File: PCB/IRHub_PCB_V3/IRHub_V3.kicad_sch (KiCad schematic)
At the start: 85 parts, among them Q1 UMH3N, SW1 SW_Push, U1 DRV2605LDGS

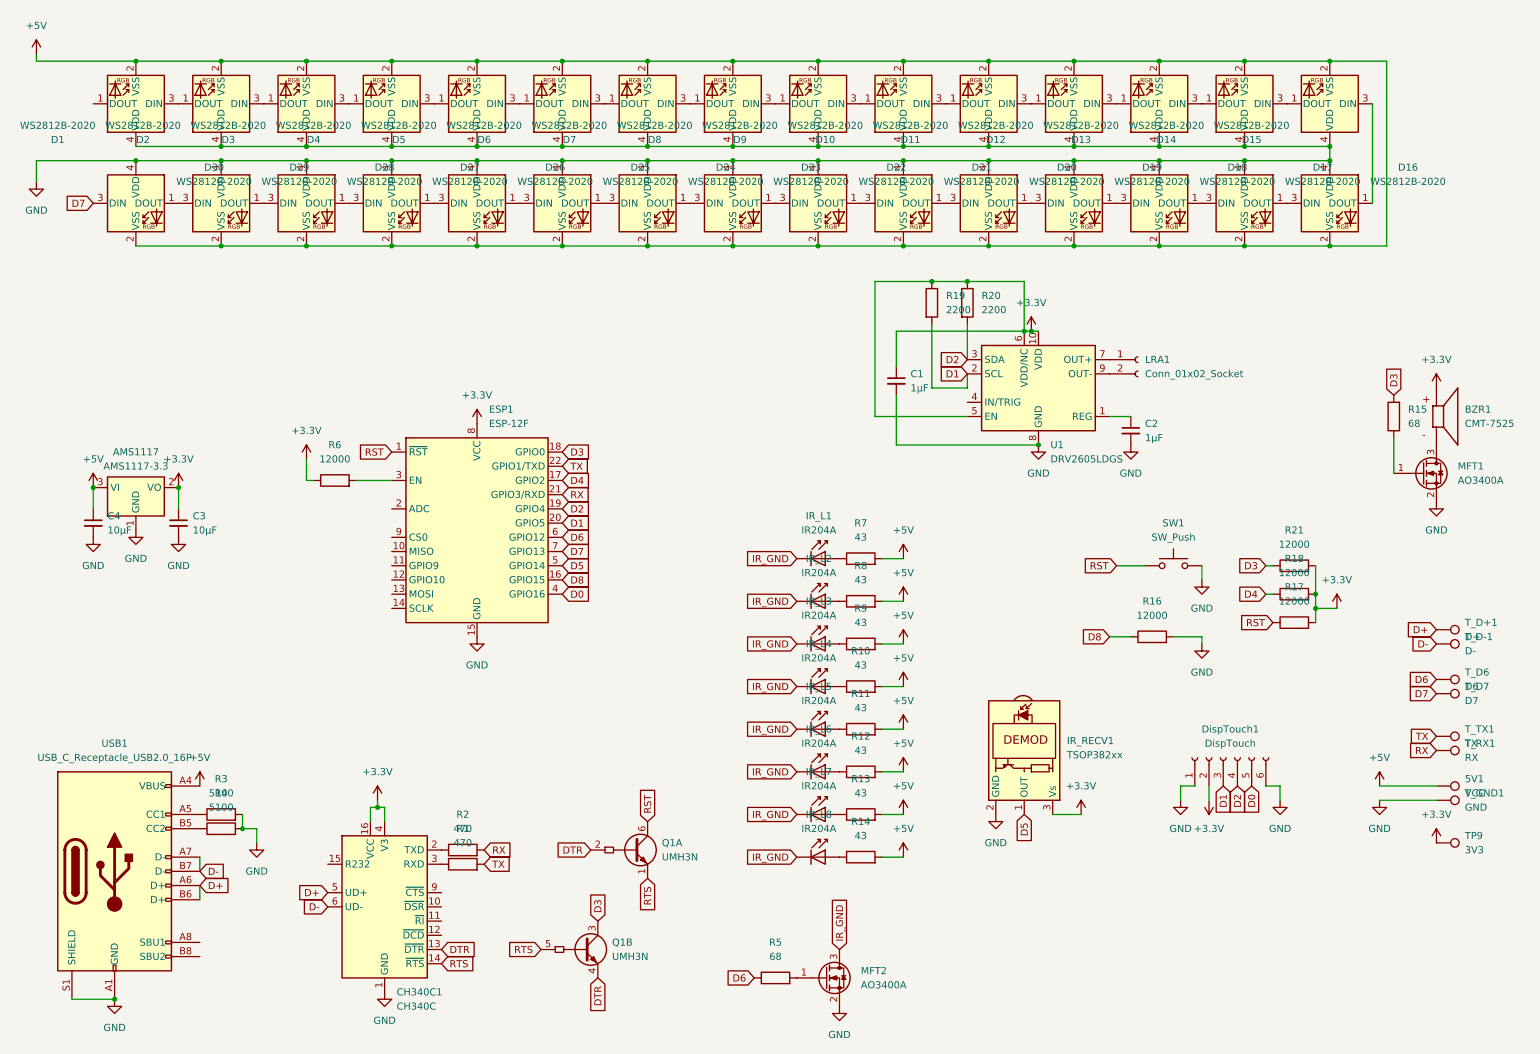
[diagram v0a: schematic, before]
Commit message: fix pcb led issue :)
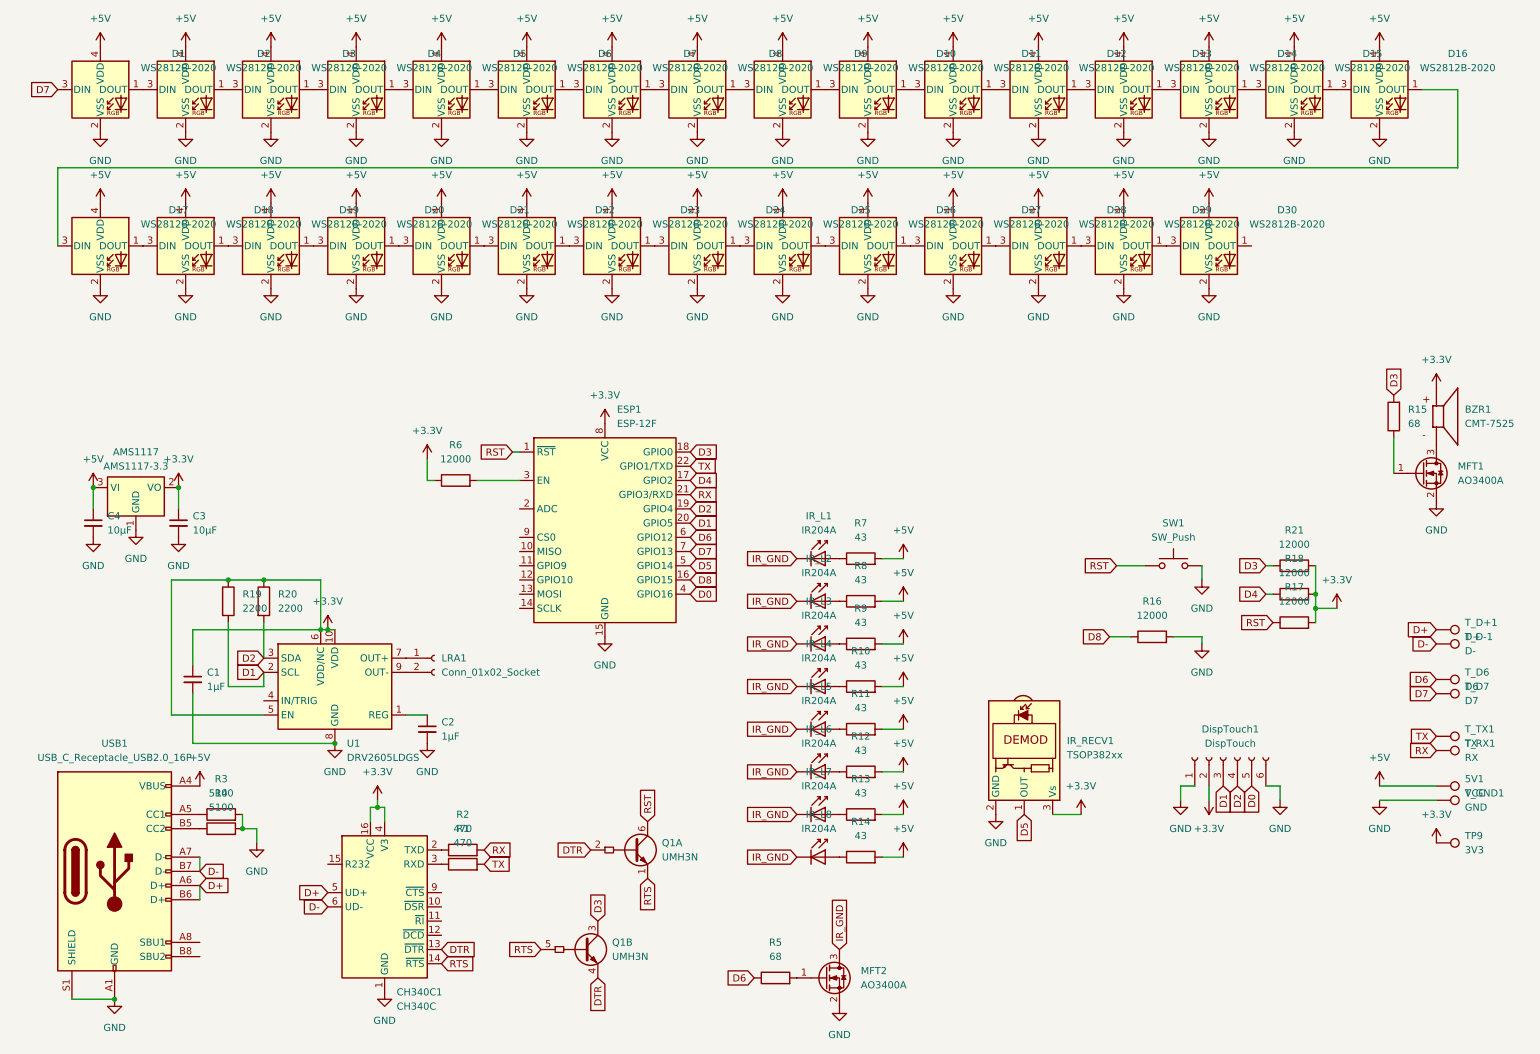
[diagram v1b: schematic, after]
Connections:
- net +5V: now also D1.4 (VDD), D10.4 (VDD), D11.4 (VDD), D12.4 (VDD), D13.4 (VDD), D14.4 (VDD), D15.4 (VDD), D16.4 (VDD), D17.4 (VDD), D18.4 (VDD), D19.4 (VDD), D2.4 (VDD), D20.4 (VDD), D21.4 (VDD), D22.4 (VDD), D23.4 (VDD), D24.4 (VDD), D25.4 (VDD), D26.4 (VDD), D27.4 (VDD), D28.4 (VDD), D29.4 (VDD), D3.4 (VDD), D30.4 (VDD), D4.4 (VDD), D5.4 (VDD), D6.4 (VDD), D7.4 (VDD), D8.4 (VDD), D9.4 (VDD); no longer D1.2 (VSS), D10.2 (VSS), D11.2 (VSS), D12.2 (VSS), D13.2 (VSS), D14.2 (VSS), D15.2 (VSS), D16.2 (VSS), D17.2 (VSS), D18.2 (VSS), D19.2 (VSS), D2.2 (VSS), D20.2 (VSS), D21.2 (VSS), D22.2 (VSS), D23.2 (VSS), D24.2 (VSS), D25.2 (VSS), D26.2 (VSS), D27.2 (VSS), D28.2 (VSS), D29.2 (VSS), D3.2 (VSS), D30.2 (VSS), D4.2 (VSS), D5.2 (VSS), D6.2 (VSS), D7.2 (VSS), D8.2 (VSS), D9.2 (VSS)
- net D7: now also D1.3 (DIN); no longer D30.3 (DIN)
- net GND: now also D1.2 (VSS), D10.2 (VSS), D11.2 (VSS), D12.2 (VSS), D13.2 (VSS), D14.2 (VSS), D15.2 (VSS), D16.2 (VSS), D17.2 (VSS), D18.2 (VSS), D19.2 (VSS), D2.2 (VSS), D20.2 (VSS), D21.2 (VSS), D22.2 (VSS), D23.2 (VSS), D24.2 (VSS), D25.2 (VSS), D26.2 (VSS), D27.2 (VSS), D28.2 (VSS), D29.2 (VSS), D3.2 (VSS), D30.2 (VSS), D4.2 (VSS), D5.2 (VSS), D6.2 (VSS), D7.2 (VSS), D8.2 (VSS), D9.2 (VSS); no longer D1.4 (VDD), D10.4 (VDD), D11.4 (VDD), D12.4 (VDD), D13.4 (VDD), D14.4 (VDD), D15.4 (VDD), D16.4 (VDD), D17.4 (VDD), D18.4 (VDD), D19.4 (VDD), D2.4 (VDD), D20.4 (VDD), D21.4 (VDD), D22.4 (VDD), D23.4 (VDD), D24.4 (VDD), D25.4 (VDD), D26.4 (VDD), D27.4 (VDD), D28.4 (VDD), D29.4 (VDD), D3.4 (VDD), D30.4 (VDD), D4.4 (VDD), D5.4 (VDD), D6.4 (VDD), D7.4 (VDD), D8.4 (VDD), D9.4 (VDD)
- net at D29.1 (DOUT): now also D30.3 (DIN); no longer D28.3 (DIN)
- net at D29.3 (DIN): now also D28.1 (DOUT); no longer D30.1 (DOUT)
- net at D1.1 (DOUT): now also D2.3 (DIN)
- net at D2.1 (DOUT): now also D3.3 (DIN); no longer D1.3 (DIN)
- net at D19.1 (DOUT): now also D20.3 (DIN); no longer D18.3 (DIN)
- net at D20.1 (DOUT): now also D21.3 (DIN); no longer D19.3 (DIN)
- net at D8.1 (DOUT): now also D9.3 (DIN); no longer D7.3 (DIN)
- net at D9.1 (DOUT): now also D10.3 (DIN); no longer D8.3 (DIN)
- net at D17.3 (DIN): now also D16.1 (DOUT); no longer D18.1 (DOUT)
- net at D21.1 (DOUT): now also D22.3 (DIN); no longer D20.3 (DIN)
- net at D26.3 (DIN): now also D25.1 (DOUT); no longer D27.1 (DOUT)
- net at D27.3 (DIN): now also D26.1 (DOUT); no longer D28.1 (DOUT)
- net at D10.1 (DOUT): now also D11.3 (DIN); no longer D9.3 (DIN)
- net at D11.1 (DOUT): now also D12.3 (DIN); no longer D10.3 (DIN)
- net at D6.3 (DIN): now also D5.1 (DOUT); no longer D7.1 (DOUT)
- net at D13.1 (DOUT): now also D14.3 (DIN); no longer D12.3 (DIN)
- net at D14.1 (DOUT): now also D15.3 (DIN); no longer D13.3 (DIN)
- net at D5.3 (DIN): now also D4.1 (DOUT); no longer D6.1 (DOUT)
- net at D23.3 (DIN): now also D22.1 (DOUT); no longer D24.1 (DOUT)
- net at D24.3 (DIN): now also D23.1 (DOUT); no longer D25.1 (DOUT)
- net at D3.1 (DOUT): now also D4.3 (DIN); no longer D2.3 (DIN)
- net at D15.1 (DOUT): now also D16.3 (DIN); no longer D14.3 (DIN)
- net at D12.1 (DOUT): now also D13.3 (DIN); no longer D11.3 (DIN)
- net at D25.3 (DIN): now also D24.1 (DOUT); no longer D26.1 (DOUT)
- net at D17.1 (DOUT): now also D18.3 (DIN); no longer D16.3 (DIN)
- new net: D6.1 (DOUT), D7.3 (DIN)
- new net: D27.1 (DOUT), D28.3 (DIN)
- new net: D7.1 (DOUT), D8.3 (DIN)
- new net: D18.1 (DOUT), D19.3 (DIN)
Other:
- moved on the sheet: C1, C2, ESP1, LRA1, R19, R20, R6, U1

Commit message: new updated version with oled connector
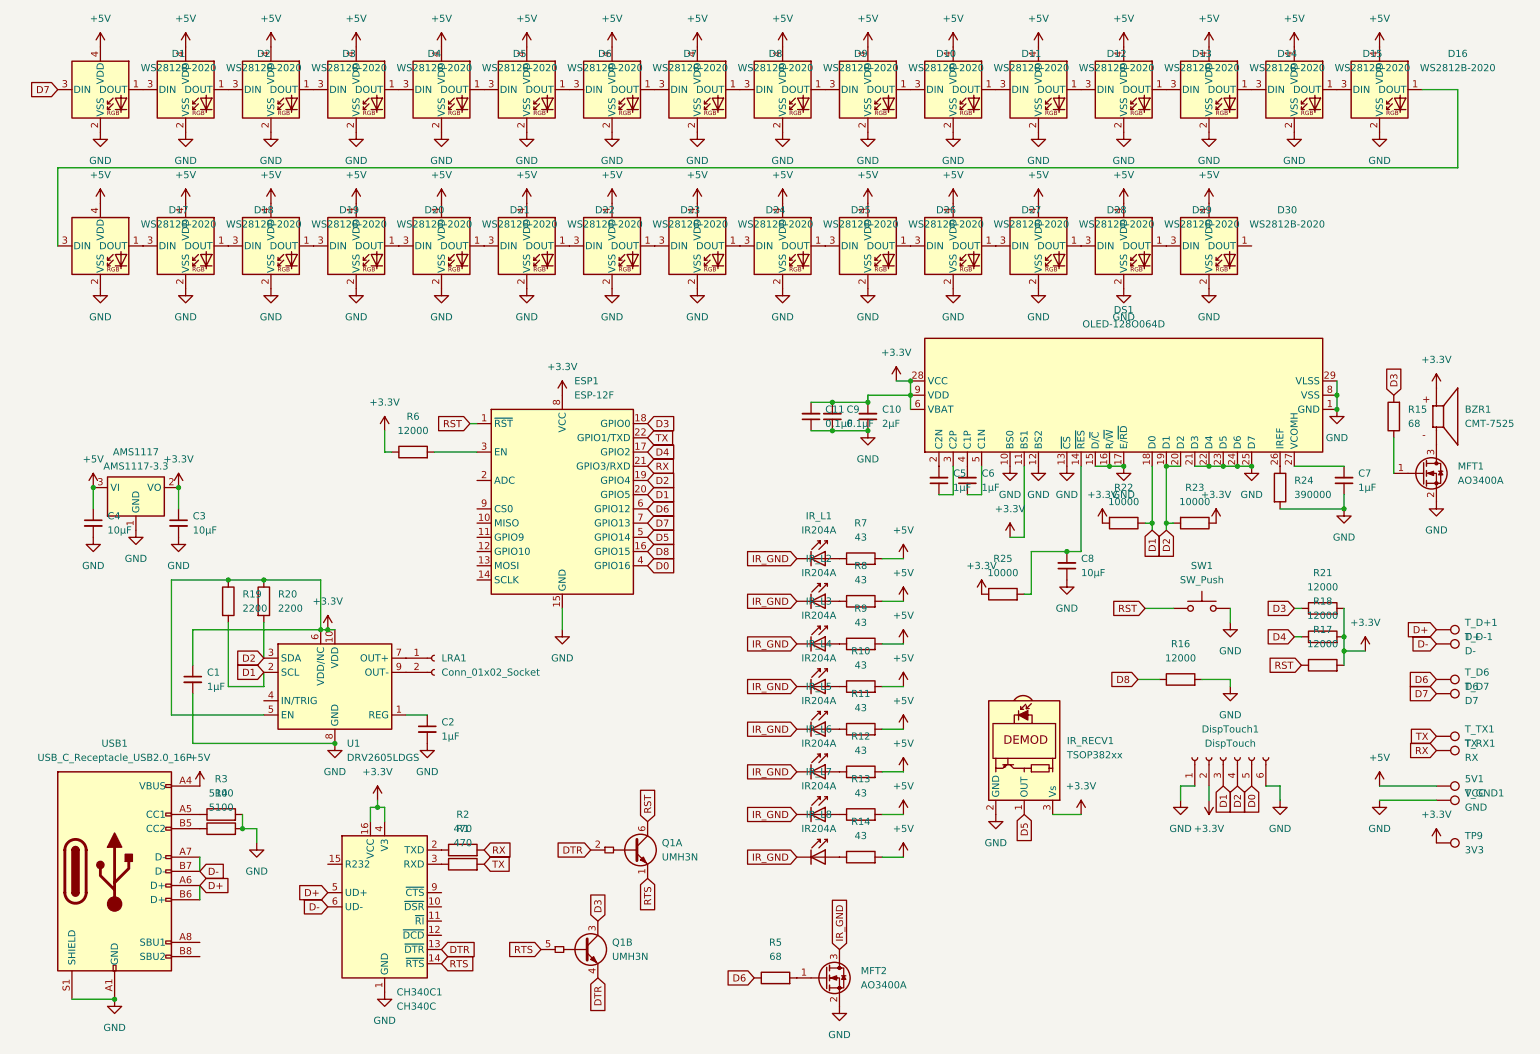
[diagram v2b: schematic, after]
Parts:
- added C10: 2µF, Capacitor_SMD:C_0805_2012Metric_Pad1.18x1.45mm_HandSolder, symbol Device:C_Small
- added C11, C9: 0.1µF, Capacitor_SMD:C_0805_2012Metric_Pad1.18x1.45mm_HandSolder, symbol Device:C_Small
- added C5, C6, C7: 1µF, Capacitor_SMD:C_0805_2012Metric_Pad1.18x1.45mm_HandSolder, symbol Device:C_Small
- added C8: 10µF, Capacitor_SMD:C_0805_2012Metric_Pad1.18x1.45mm_HandSolder, symbol Device:C_Small
- added DS1: OLED-128O064D, Display:OLED-128O064D, symbol Display_Graphic:OLED-128O064D
- added R22, R23, R25: 10000, Resistor_SMD:R_0805_2012Metric_Pad1.20x1.40mm_HandSolder, symbol Device:R
- added R24: 390000, Resistor_SMD:R_0805_2012Metric_Pad1.20x1.40mm_HandSolder, symbol Device:R
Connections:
- net +3.3V: now also C10.2, C11.2, C9.2, DS1.11 (BS1), DS1.28 (VCC), DS1.6 (VBAT), DS1.9 (VDD), R22.2, R23.1, R25.1
- net D1: now also DS1.18 (D0), R22.1
- net D2: now also DS1.19 (D1), DS1.20 (D2), R23.2
- net GND: now also C10.1, C11.1, C7.1, C8.1, C9.1, DS1.1 (GND), DS1.10 (BS0), DS1.12 (BS2), DS1.13 (~{CS}), DS1.15 (D/~{C}), DS1.16 (R/~{W}), DS1.17 (E/~{RD}), DS1.21 (D3), DS1.22 (D4), DS1.23 (D5), DS1.24 (D6), DS1.25 (D7), DS1.29 (VLSS), DS1.30 (GND), DS1.8 (VSS), R24.2
- new net: C5.1, DS1.3 (C2P)
- new net: C5.2, DS1.2 (C2N)
- new net: C7.2, DS1.27 (VCOMH)
- new net: C8.2, DS1.14 (~{RES}), R25.2
- new net: DS1.26 (IREF), R24.1
- new net: C6.2, DS1.4 (C1P)
- new net: C6.1, DS1.5 (C1N)
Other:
- moved on the sheet: ESP1, R16, R17, R18, R21, R6, SW1

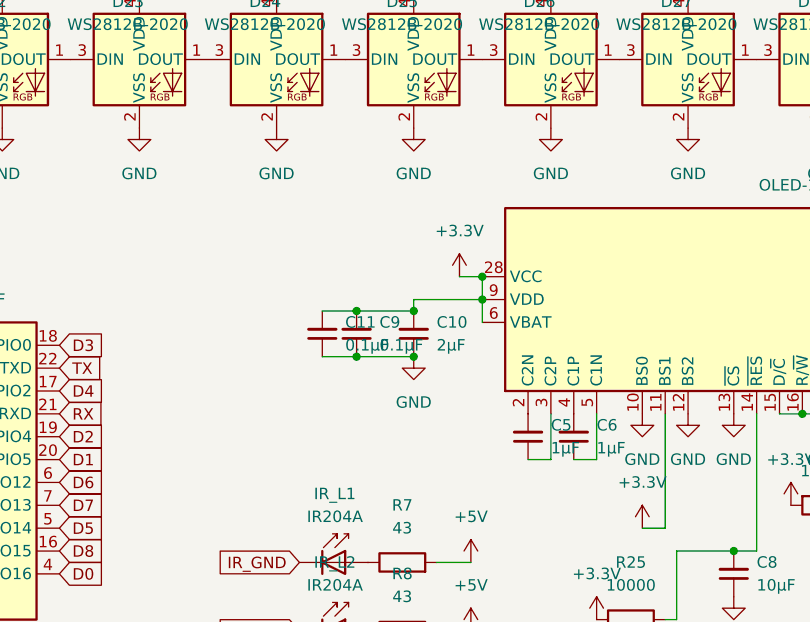
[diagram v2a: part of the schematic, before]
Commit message: fix oled connector wiring
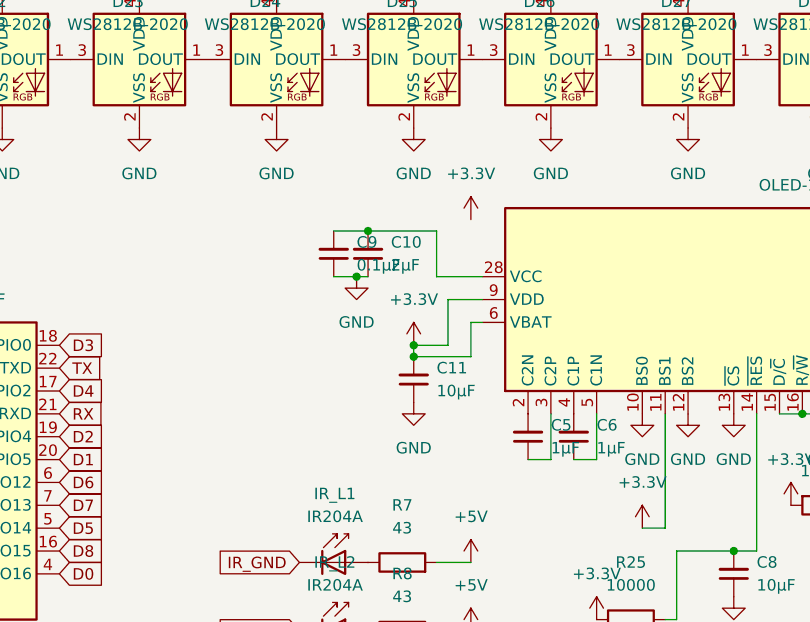
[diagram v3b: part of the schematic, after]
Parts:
- C11: value 0.1µF -> 10µF
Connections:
- net +3.3V: no longer C10.2, C9.2, DS1.28 (VCC)
- new net: C10.2, C9.2, DS1.28 (VCC)
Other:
- moved on the sheet: C9
